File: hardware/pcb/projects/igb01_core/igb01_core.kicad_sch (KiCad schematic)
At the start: 111 parts, among them J1 BAT_CON, J10 STMP157_GPIO2, J11 STMP157_GPIO3, J12 JTAG, J13 STMP157_GPIO4, J14 Micro_SD_Card, J15 PWR_ON_CON, J16 STMP157_GPIO5, J17 USB_CONN, J18 FPA-VZA2-15-LF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

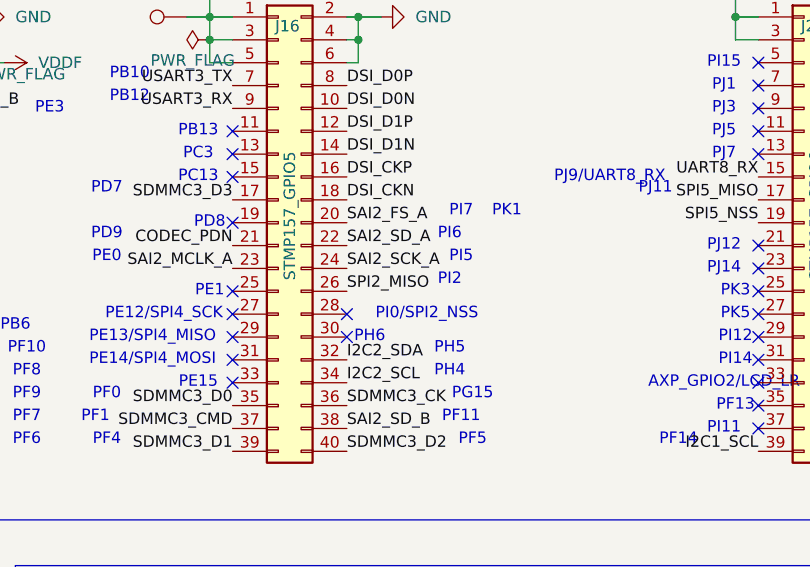
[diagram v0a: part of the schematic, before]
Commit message: connect all pads for core pcb
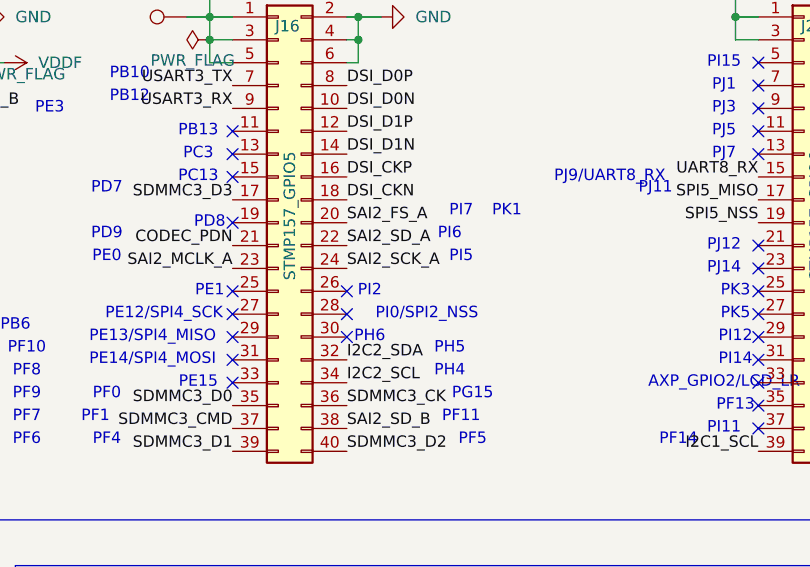
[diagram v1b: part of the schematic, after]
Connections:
- net SPI2_MISO: no longer J16.26 (Pin_26)
- no-connect marks 112 -> 113
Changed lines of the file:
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@@
 	(text "PI2"
 		(exclude_from_sim no)
-		(at 316.23 68.58 0)
+		(at 307.34 69.85 0)
 		(effects
 			(font
@@
 	)
 	(no_connect
+		(at 304.8 69.85)
+	)
+	(no_connect
 		(at 246.38 59.69)
 	)
@@
 		)
 	)
-	(label "SPI2_MISO"
-		(at 304.8 69.85 0)
-		(effects
-			(font
-				(size 1.27 1.27)
-			)
-			(justify left bottom)
-		)
-	)

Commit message: update igb01 core board & create gerber files
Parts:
- SW1: footprint Package_DIP:SMDIP-8_W9.53mm -> custom:DIP_Switch_1.27mm_SMD
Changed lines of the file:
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@@
 			)
 		)
-		(property "Footprint" "Package_DIP:SMDIP-8_W9.53mm"
+		(property "Footprint" "custom:DIP_Switch_1.27mm_SMD"
 			(at 38.1 210.82 0)
 			(effects

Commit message: add schematic pdfs
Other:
- title: (none) -> igb_core
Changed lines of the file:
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@@
 	(generator_version "9.0")
 	(paper "A3")
+	(title_block
+		(title "igb_core")
+		(rev "0.1")
+	)
 	(rectangle
 		(start 201.93 100.33)
